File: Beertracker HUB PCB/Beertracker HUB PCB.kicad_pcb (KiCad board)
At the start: 2 copper layers, 63.5 x 61.5 mm, 17 parts, among them J1 Conn_01x08_Pin - RC522 RFID, J2 Conn_01x04_Pin - I2C LCD, J3 Conn_01x03_Socket - DHT11, SW1 SW_Push - minus, SW2 SW_Push - Plus, U1 ESP32_NODEMCU

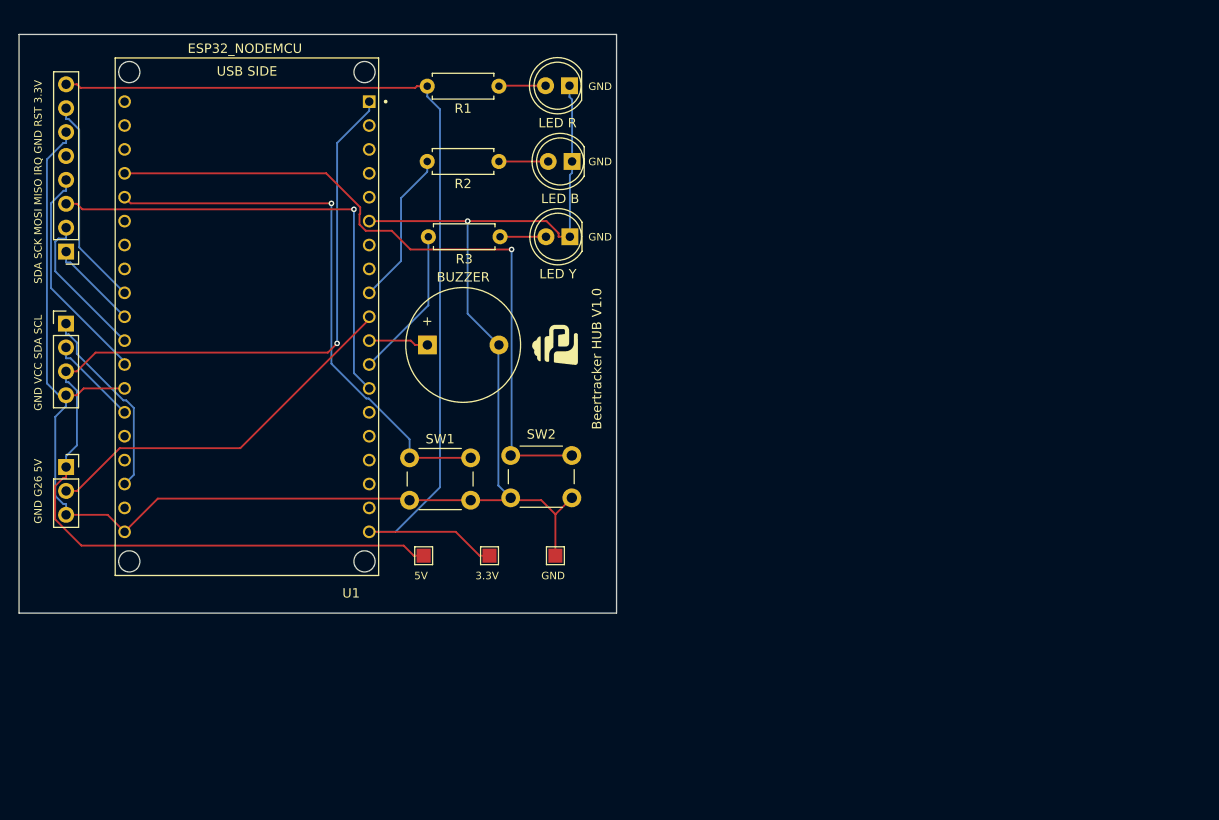
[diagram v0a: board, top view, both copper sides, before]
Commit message: finalized and ordered PCB design, changed code to be OLED screen orientated
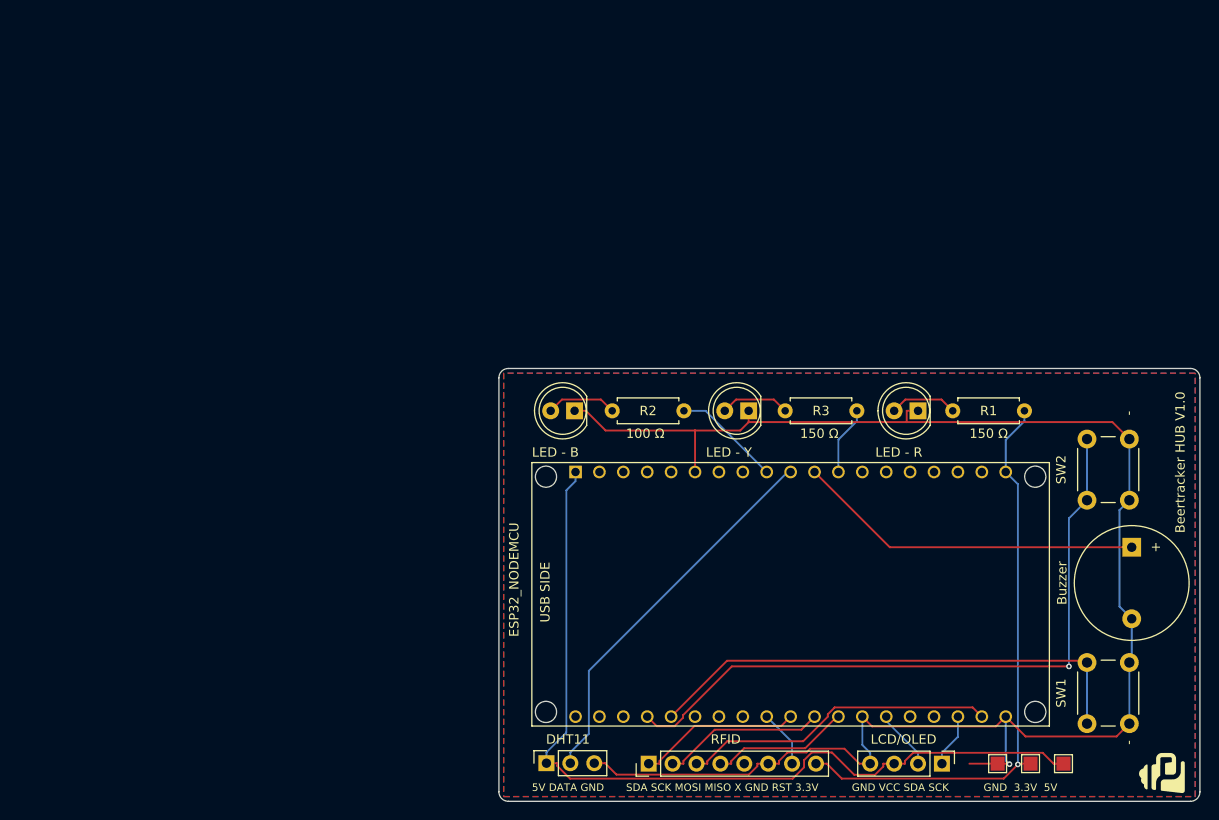
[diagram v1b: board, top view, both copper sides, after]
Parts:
- removed BUZZER: Buzzer, Buzzer_Beeper:Buzzer_12x9.5RM7.6
- removed LED B: LED - B, LED_THT:LED_D5.0mm
- removed LED R: LED - R, LED_THT:LED_D5.0mm
- removed LED Y: LED - Y, LED_THT:LED_D5.0mm
- added BZ1: Buzzer, Buzzer_Beeper:Buzzer_12x9.5RM7.6, F.Cu at (163.8, 81.0)
- added D1: LED - R, LED_THT:LED_D5.0mm, F.Cu at (141.0, 66.5)
- added D2: LED - B, LED_THT:LED_D5.0mm, F.Cu at (104.5, 66.5)
- added D3: LED - Y, LED_THT:LED_D5.0mm, F.Cu at (123.0, 66.5)
- moved J2 104.2 mm to (143.6, 104.0), turned to -90 degrees
- moved J1 82.4 mm to (112.4, 104.0), turned to 90 degrees
- moved G*** 78.9 mm to (167.0, 105.0)
- moved SW1 77.3 mm to (159.0, 99.8), turned to 90 degrees
- moved TP3 71.5 mm to (156.5, 104.0), turned to 180 degrees
- moved U1 64.9 mm to (127.5, 86.0), turned to -90 degrees
- moved TP2 61.6 mm to (153.0, 104.0), turned to 180 degrees
- moved J3 60.0 mm to (101.5, 104.0), turned to 90 degrees
- moved SW2 59.6 mm to (163.5, 69.5), turned to -90 degrees
- moved R1 59.3 mm to (144.7, 66.5), turned to 0 degrees
- moved TP1 51.9 mm to (149.5, 104.0), turned to 180 degrees
- moved R3 35.5 mm to (126.9, 66.5), turned to 0 degrees
- moved R2 29.1 mm to (108.5, 66.5), turned to 0 degrees
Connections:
- U1 pad J4_2: unconnected-(U1-G23-PadJ4_2) -> Net-(J1-Pin_3)
- U1 pad J5_13: Net-(J1-Pin_3) -> unconnected-(U1-G32-PadJ5_13)
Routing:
- net +3.3V: track 105.1 -> 63.1 mm, vias 0 -> 1
- net Net-(BZ1-+): track 6.38 -> 37.0 mm
- net +5V: track 115.4 -> 92.4 mm, vias 1 -> 0
- net Net-(J1-Pin_3): track 50.5 -> 33.5 mm, vias 1 -> 0
- net Net-(J1-Pin_7): track 22.4 -> 6.12 mm
- net Net-(J2-Pin_1): track 20.8 -> 5.70 mm
- net Net-(J1-Pin_4): track 23.7 -> 14.8 mm
- net Net-(U1-G33): track 16.2 -> 7.31 mm
- net Net-(J1-Pin_1): track 9.76 -> 17.3 mm
- net Net-(U1-G2): track 59.4 -> 53.2 mm, vias 1 -> 0
- net GND: track 183.5 -> 177.8 mm
- net Net-(U1-G27): track 16.5 -> 11.5 mm
- net Net-(J2-Pin_2): track 9.76 -> 6.40 mm
- net Net-(D3-A): track 4.88 -> 7.42 mm
- net Net-(D2-A): track 5.23 -> 7.54 mm
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- added copper zone on B.Cu, net GND
- added copper zone on F.Cu, net GND
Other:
- board size 63.5 x 61.5 mm -> 74.5 x 46 mm
- board text added: "-"
- board text added: "100 Ω"
- board text added: "150 Ω"
- board text added: "5V DATA GND"
- board text added: "DHT11"
- board text added: "Designed by Lars Grit"
- board text added: "GND 3.3V 5V"
- board text added: "GND VCC SDA SCK"
- board text added: "LCD/OLED"
- board text added: "LED - B"
- board text added: "LED - R"
- board text added: "LED - Y"
- board text added: "RFID"
- board text added: "SDA SCK MOSI MISO X GND RST 3.3V"
- board text added: "www.beertracker.com"
- board text removed: "3.3V"
- board text removed: "5V"
- board text removed: "FLIP ME OVER >:(((("
- board text removed: "GND"
- board text removed: "GND G26 5V"
- board text removed: "GND VCC SDA SCL"
- board text removed: "SDA SCK MOSI MISO IRQ GND RST 3.3V"
